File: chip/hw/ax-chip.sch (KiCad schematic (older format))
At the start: 75 parts, among them IC1 CHIPv1_0, IC2 TPS73433, IC3 AX5043, IC4 TG-5006CJ, J1 CONN_01x02, J2 CONN_01x02, P1 PAD, P2 COAX, P3 COAX, P5 PAD, Q1 NX7002AK, U1 DS2401P, X1 CONN, X2 CONN

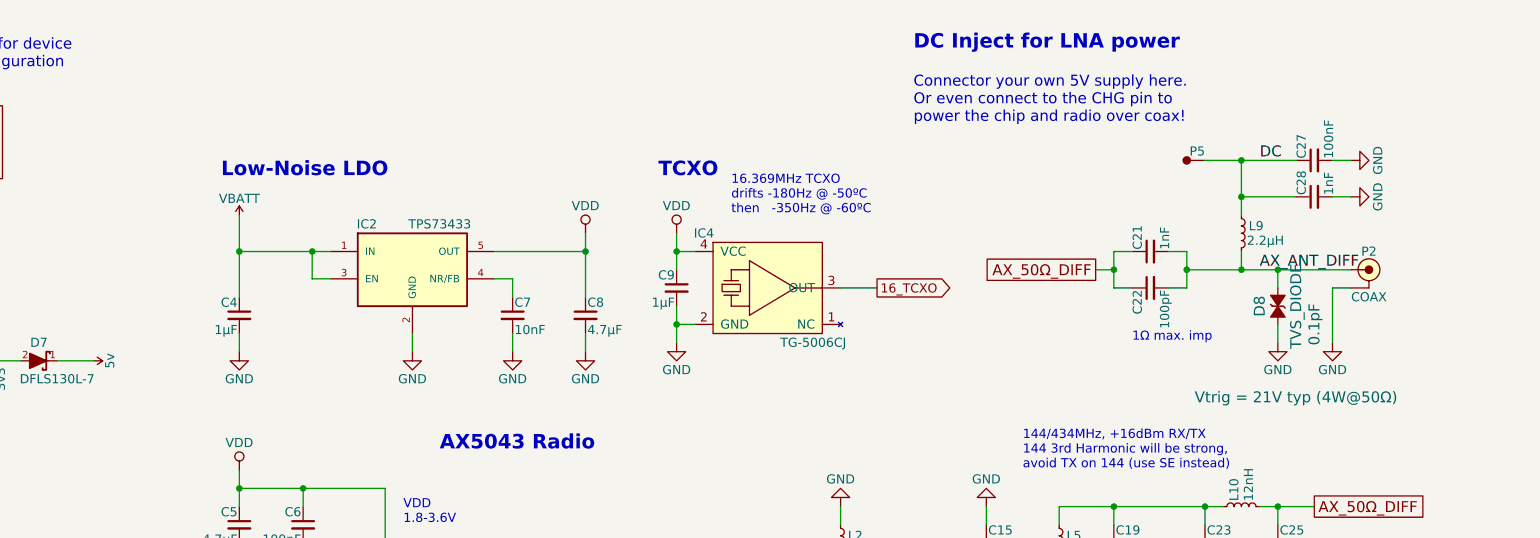
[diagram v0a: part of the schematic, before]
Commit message: [chip hw] add LNA, remove dc power inject
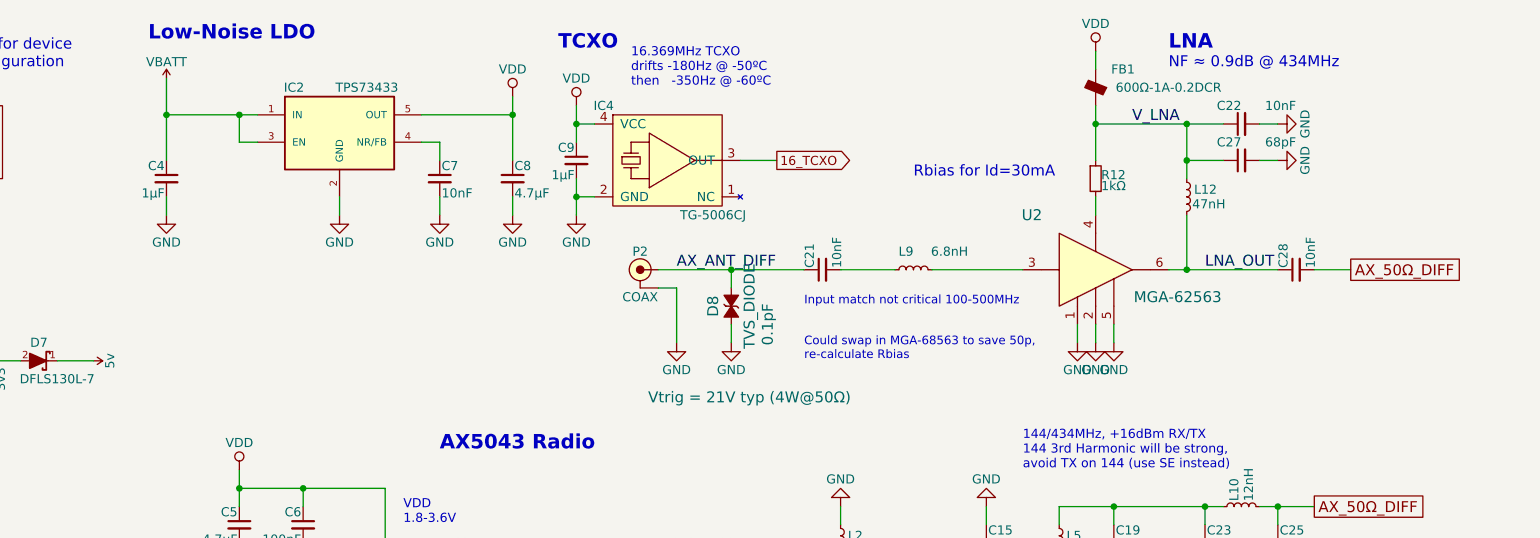
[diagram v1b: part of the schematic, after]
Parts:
- removed P5: PAD, agg:WIREPAD, symbol PAD
- added FB1: 600Ω-1A-0.2DCR, agg:0603, symbol BEAD
- added L12: 47nH, agg:0402, symbol L_Small
- added R12: 1kΩ, agg:0402, symbol R_Small
- added U2: MGA-62563, TO_SOT_Packages_SMD:SC-70-6, symbol MGA-68563
- C21, C28: value 1nF -> 10nF; Farnell (none) -> 8819734; STD.PAS 1nF -> (none)
- C22: value 100pF -> 10nF; STD.PAS 100pF -> 10nF
- C27: value 100nF -> 68pF; STD.PAS 100nF -> 68pF
- L1: footprint agg:0402 -> agg:0603
- L9: value 2.2µH -> 6.8nH; footprint agg:0805 -> agg:0402; Digikey (none) -> 490-6840-1-ND; Farnell 2345130 -> 1762612
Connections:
- net AX_50Ω_DIFF: now also C28.2; no longer C21.1, C22.1
- net AX_ANT_DIFF: now also C21.1; no longer C21.2, C22.2, L9.2
- net GND: now also C22.2, U2.1, U2.2, U2.5; no longer C28.2
- net VDD: now also FB1.1
- removed net DC: C27.1, C28.1, L9.1
- new net: C21.2, L9.1
- new net: L9.2, U2.3
- new net: R12.2, U2.4
- new net LNA_OUT: C28.1, L12.2, U2.6
- new net V_LNA: C22.1, C27.1, FB1.2, L12.1, R12.1
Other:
- note added: "Could swap in MGA-68563 to save 50p,\nre-calculate Rbias"
- note added: "Input match not critical 100-500MHz"
- note added: "LNA"
- note added: "NF ≈ 0.9dB @ 434MHz\n"
- note added: "Rbias for Id=30mA"
- note removed: "1Ω max. imp"
- note removed: "Connector your own 5V supply here.\nOr even connect to the CHG pin to\npower the chip and radio over coax!"
- note removed: "DC Inject for LNA power"
- moved on the sheet: C21, C4, C7, C8, C9, D8, IC2, IC4, P2
